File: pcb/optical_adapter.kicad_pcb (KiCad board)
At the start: 2 copper layers, 50 x 20 mm, 15 parts, among them J1 Conn_01x06_Pin, Q1 BC847, Q2 BC847, Q3 BC857, Q4 BC817, U1 LM1117MP-3.3

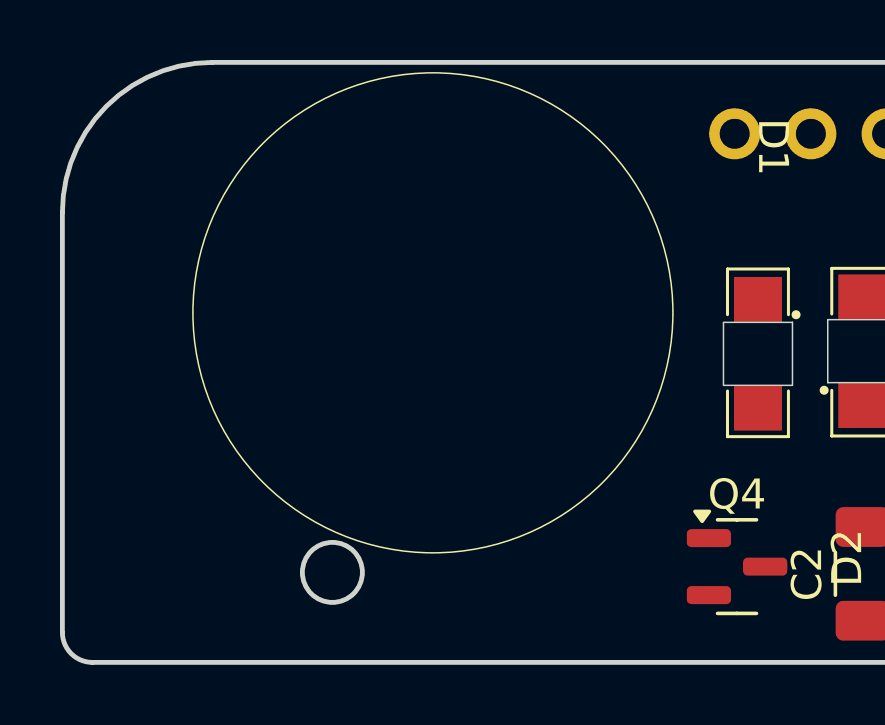
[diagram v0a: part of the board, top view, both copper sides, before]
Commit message: Add PCB coil footprint
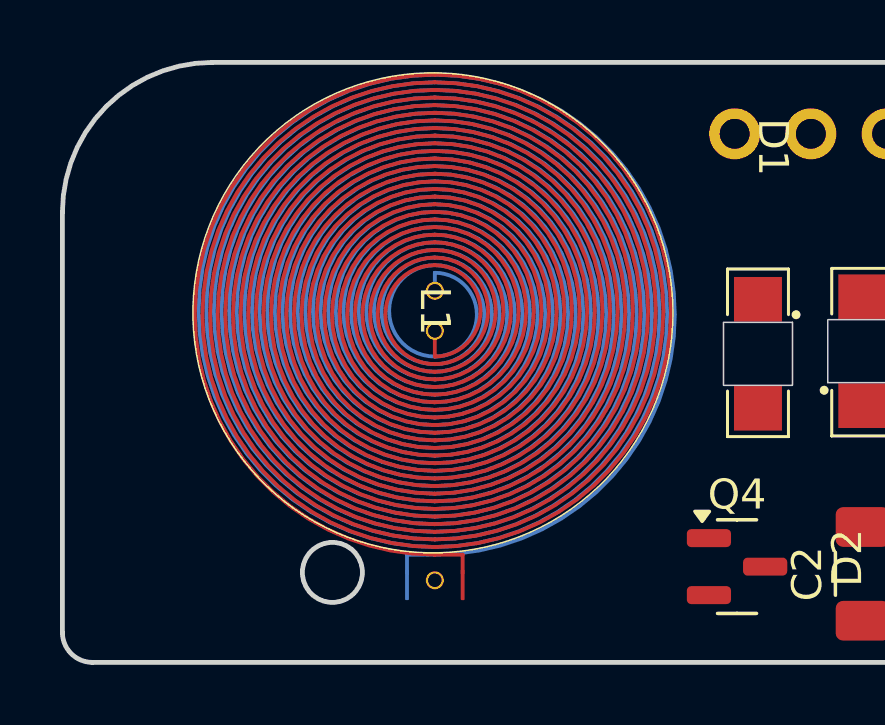
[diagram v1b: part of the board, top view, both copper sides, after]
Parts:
- added L1: L, footprints:26_turn_16_dia_5_mil, F.Cu at (117.0, 95.9)

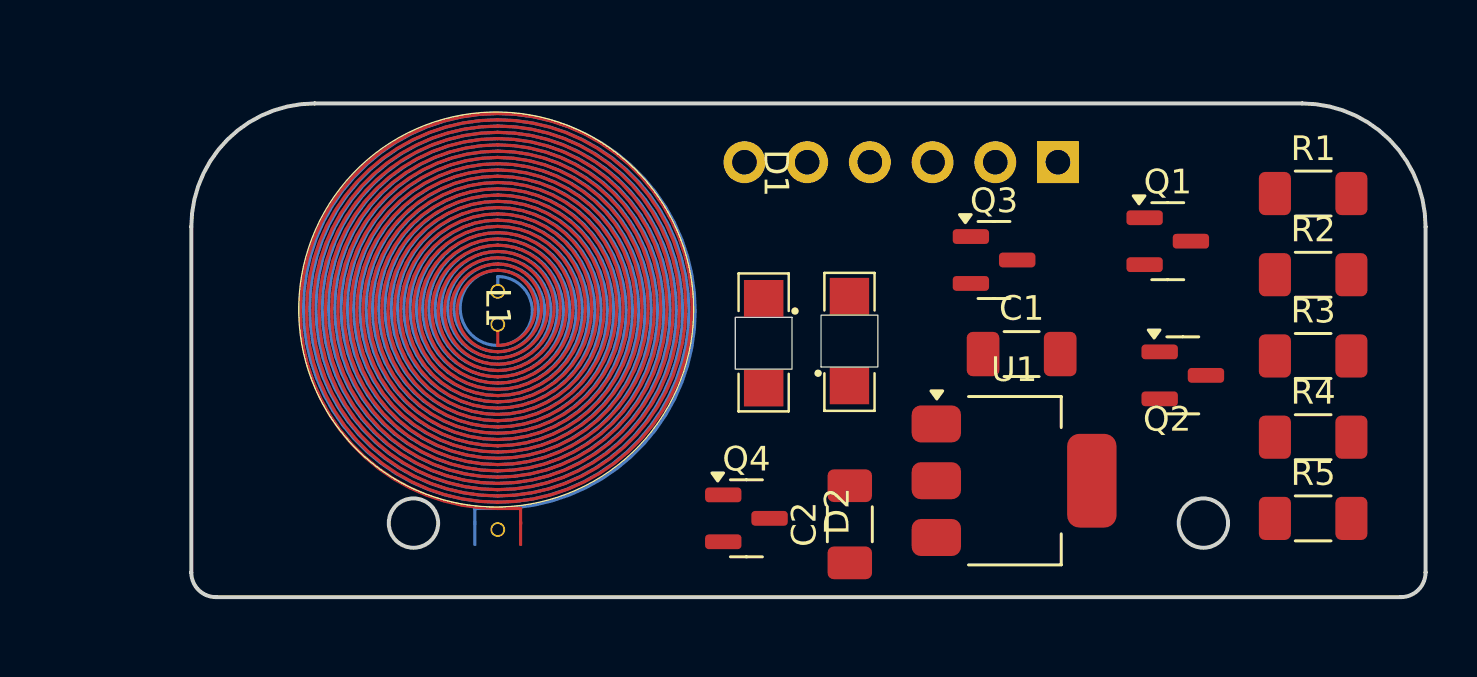
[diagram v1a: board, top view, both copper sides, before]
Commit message: Rough PCB component layout
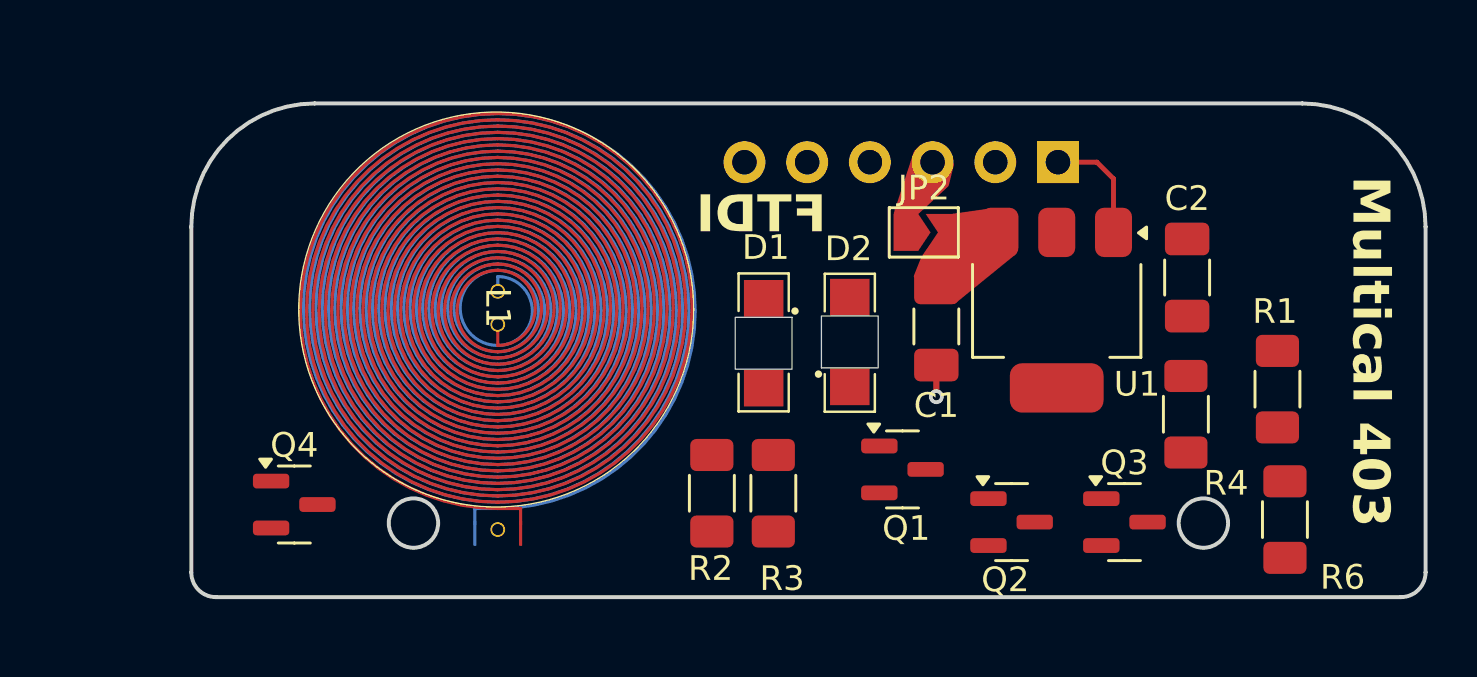
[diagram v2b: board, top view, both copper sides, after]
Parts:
- removed R5: R, Resistor_SMD:R_1206_3216Metric_Pad1.30x1.75mm_HandSolder
- added JP2: SolderJumper_2_Bridged, Jumper:SolderJumper-2_P1.3mm_Open_TrianglePad1.0x1.5mm, F.Cu at (134.2, 92.8)
- added R6: 10k, Resistor_SMD:R_1206_3216Metric_Pad1.30x1.75mm_HandSolder, F.Cu at (148.8, 104.4)
- R1: value R -> 100
- R2: value R -> 15k
- R3: value R -> 39k
- R4: value R -> 10k
- moved R2 25.9 mm to (125.6, 103.4), turned to -90 degrees
- moved R3 22.6 mm to (128.1, 103.4), turned to -90 degrees
- moved Q4 18.3 mm to (108.7, 103.8)
- moved C2 16.9 mm to (144.9, 94.6)
- moved Q1 14.2 mm to (133.3, 102.4)
- moved Q3 11.9 mm to (142.3, 104.5)
- moved Q2 9.13 mm to (137.8, 104.5)
- moved R1 8.06 mm to (148.5, 99.2), turned to 90 degrees
- moved U1 7.12 mm to (139.6, 96.0), turned to -90 degrees
- moved R4 5.24 mm to (144.8, 100.2), turned to -90 degrees
- moved C1 3.63 mm to (134.7, 96.6), turned to -90 degrees
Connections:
- C1 pad 1: unconnected-(C1-Pad1) -> +5V
- C1 pad 2: unconnected-(C1-Pad2) -> GND
- C2 pad 1: unconnected-(C2-Pad1) -> +3V3
- C2 pad 2: unconnected-(C2-Pad2) -> GND
- D1 pad 1: unconnected-(D1-K-Pad1) -> +3V3
- D1 pad 2: unconnected-(D1-A-Pad2) -> /TX
- D2 pad 1: unconnected-(D2-K-Pad1) -> GND
- D2 pad 2: unconnected-(D2-A-Pad2) -> Net-(D2-A)
- J1 pad 3: unconnected-(J1-Pin_3-Pad3) -> VBUS
- Q1 pad 1: unconnected-(Q1-B-Pad1) -> /TX
- Q1 pad 2: unconnected-(Q1-E-Pad2) -> Net-(Q1-E)
- Q1 pad 3: unconnected-(Q1-C-Pad3) -> Net-(Q1-C)
- Q2 pad 1: unconnected-(Q2-B-Pad1) -> Net-(Q1-E)
- Q2 pad 2: unconnected-(Q2-E-Pad2) -> GND
- Q2 pad 3: unconnected-(Q2-C-Pad3) -> /RX
- Q3 pad 1: unconnected-(Q3-B-Pad1) -> Net-(Q3-B)
- Q3 pad 2: unconnected-(Q3-E-Pad2) -> +3V3
- Q3 pad 3: unconnected-(Q3-C-Pad3) -> Net-(Q3-C)
- R1 pad 1: unconnected-(R1-Pad1) -> Net-(Q3-C)
- R1 pad 2: unconnected-(R1-Pad2) -> Net-(D2-A)
- R2 pad 1: unconnected-(R2-Pad1) -> /TX
- R2 pad 2: unconnected-(R2-Pad2) -> GND
- R3 pad 1: unconnected-(R3-Pad1) -> /TX
- R3 pad 2: unconnected-(R3-Pad2) -> Net-(Q3-B)
- R4 pad 1: unconnected-(R4-Pad1) -> +3V3
- R4 pad 2: unconnected-(R4-Pad2) -> Net-(Q1-C)
- U1 pad 1: unconnected-(U1-GND-Pad1) -> GND
- U1 pad 2: unconnected-(U1-VO-Pad2) -> +3V3
- U1 pad 3: unconnected-(U1-VI-Pad3) -> +5V
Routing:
- net GND: track 0.00 -> 5.98 mm, vias 0 -> 1
- added copper zone on In2.Cu, net +3V3
- added copper zone on In1.Cu, net GND
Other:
- copper layers 2 -> 4
- board text added: "FTDI"
- board text added: "Multical 403"

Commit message: Update layout with coil driver components
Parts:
- removed Q4: BC817, Package_TO_SOT_SMD:SOT-23
- added D3: LED, LED_SMD:LED_1206_3216Metric_Pad1.42x1.75mm_HandSolder, F.Cu at (108.8, 104.3)
- added D4: LED, LED_SMD:LED_1206_3216Metric_Pad1.42x1.75mm_HandSolder, F.Cu at (145.6, 89.6)
- added Q5: IRLML2060, Package_TO_SOT_SMD:SOT-23, F.Cu at (106.9, 99.4)
- added R5: 10k, Resistor_SMD:R_1206_3216Metric_Pad1.30x1.75mm_HandSolder, F.Cu at (106.3, 94.7)
- added R7: 220, Resistor_SMD:R_1206_3216Metric_Pad1.30x1.75mm_HandSolder, F.Cu at (107.8, 90.9)
- added R8: 91, Resistor_SMD:R_1206_3216Metric_Pad1.30x1.75mm_HandSolder, F.Cu at (106.3, 104.2)
- added R9: 5.6, Resistor_SMD:R_1206_3216Metric_Pad1.30x1.75mm_HandSolder, F.Cu at (149.4, 90.9)
- moved L1 0.81 mm to (117.8, 96.0), turned to 180 degrees
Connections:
- J1 pad 2: unconnected-(J1-Pin_2-Pad2) -> /WAKE
- J1 pad 4: unconnected-(J1-Pin_4-Pad4) -> /TX
- J1 pad 5: unconnected-(J1-Pin_5-Pad5) -> /RX
- L1 pad 1: unconnected-(L1-Pad1) -> +5V
- L1 pad 2: unconnected-(L1-Pad2) -> Net-(Q5-D)
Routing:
- net VBUS: track 0.00 -> 44.9 mm, vias 0 -> 1
- net Net-(D3-A): track 0.00 -> 2.49 mm
- net GND: track 5.98 -> 8.35 mm, vias 1 -> 2
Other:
- board text removed: "FTDI"

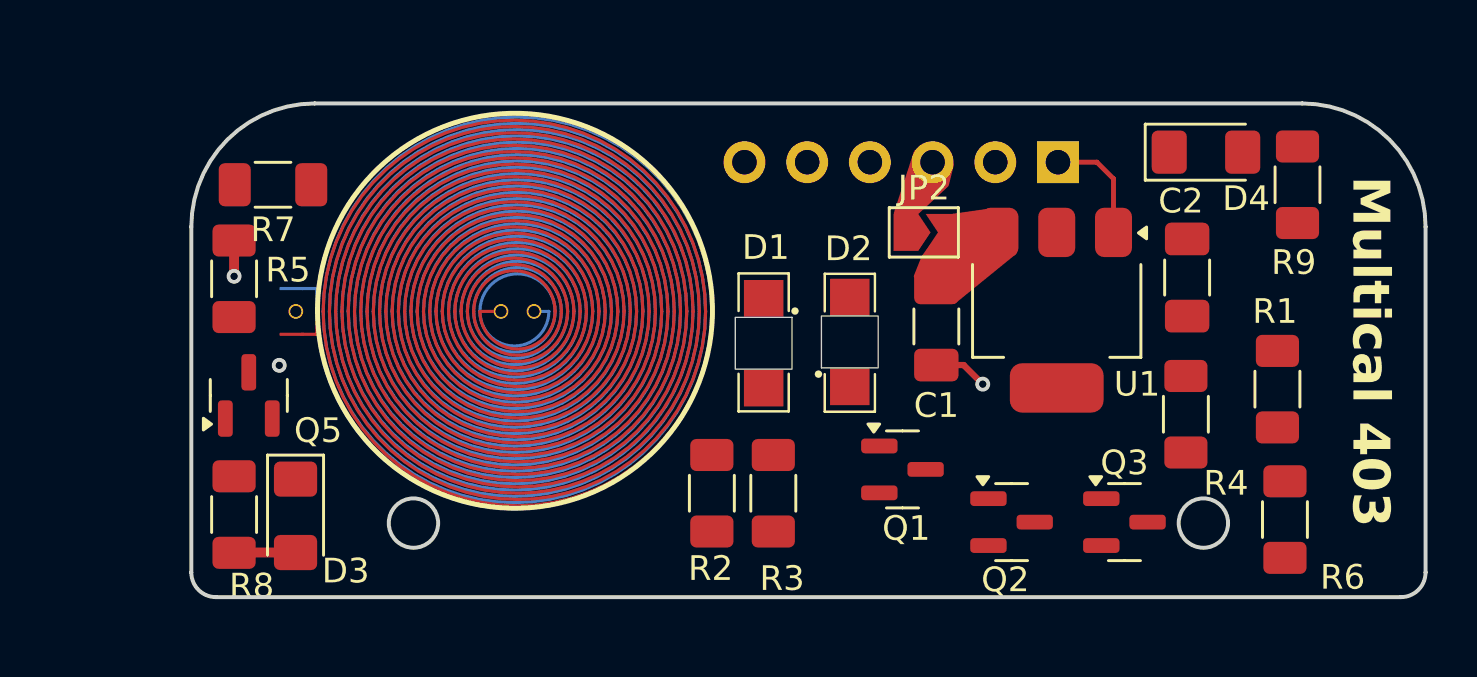
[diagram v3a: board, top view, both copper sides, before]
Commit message: Route power supply
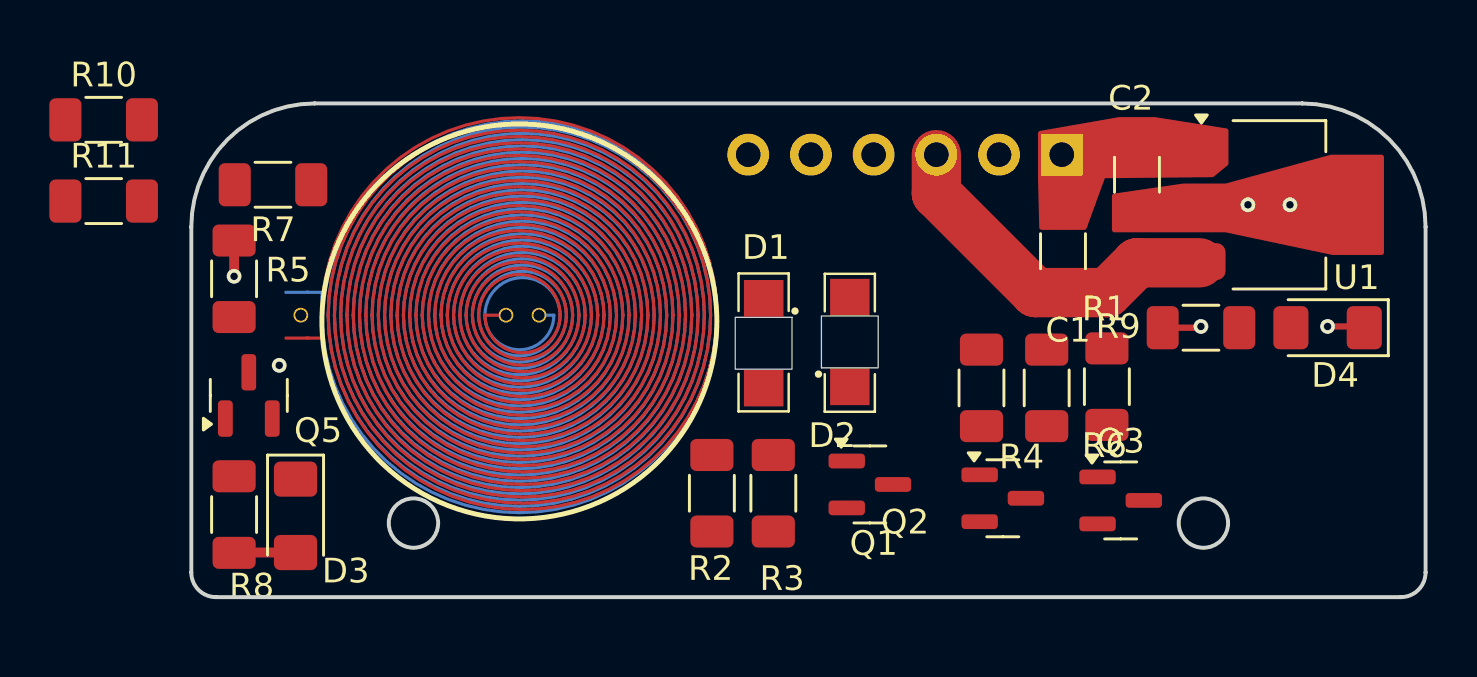
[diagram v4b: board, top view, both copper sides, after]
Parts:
- removed JP2: SolderJumper_2_Bridged, Jumper:SolderJumper-2_P1.3mm_Open_TrianglePad1.0x1.5mm
- added R10: 0, Resistor_SMD:R_1206_3216Metric_Pad1.30x1.75mm_HandSolder, F.Cu at (101.0, 88.3)
- added R11: 0, Resistor_SMD:R_1206_3216Metric_Pad1.30x1.75mm_HandSolder, F.Cu at (101.0, 91.5)
- moved R6 11.0 mm to (139.2, 99.1)
- moved U1 9.95 mm to (148.6, 91.7), turned to 0 degrees
- moved D4 8.65 mm to (150.6, 96.7), turned to 180 degrees
- moved R4 8.35 mm to (136.6, 99.1)
- moved R9 6.99 mm to (145.4, 96.7), turned to 180 degrees
- moved R1 6.91 mm to (141.6, 99.1)
- moved C1 5.97 mm to (139.9, 93.6), turned to 90 degrees
- moved C2 4.63 mm to (142.8, 90.5)
- moved Q1 1.45 mm to (132.0, 103.0)
- moved Q2 1.03 mm to (137.4, 103.6)
- moved Q3 0.89 mm to (142.2, 103.7)
- moved J1 0.34 mm to (139.8, 89.7)
- moved L1 0.25 mm to (118.0, 96.2)
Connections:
- J1 pad 3: VBUS -> +5V
- L1 pad 1: +5V -> Net-(L1-Pad1)
- L1 pad 2: Net-(Q5-D) -> Net-(L1-Pad2)
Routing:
- net +5V: track 0.00 -> 59.4 mm, vias 0 -> 1
- net VBUS: track 44.9 -> 0.00 mm, vias 1 -> 0
- net GND: track 8.35 -> 3.15 mm
- net +3V3: track 0.00 -> 1.51 mm, vias 0 -> 3
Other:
- board text removed: "Multical 403"

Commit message: Update PCB layout
All traces are routed.
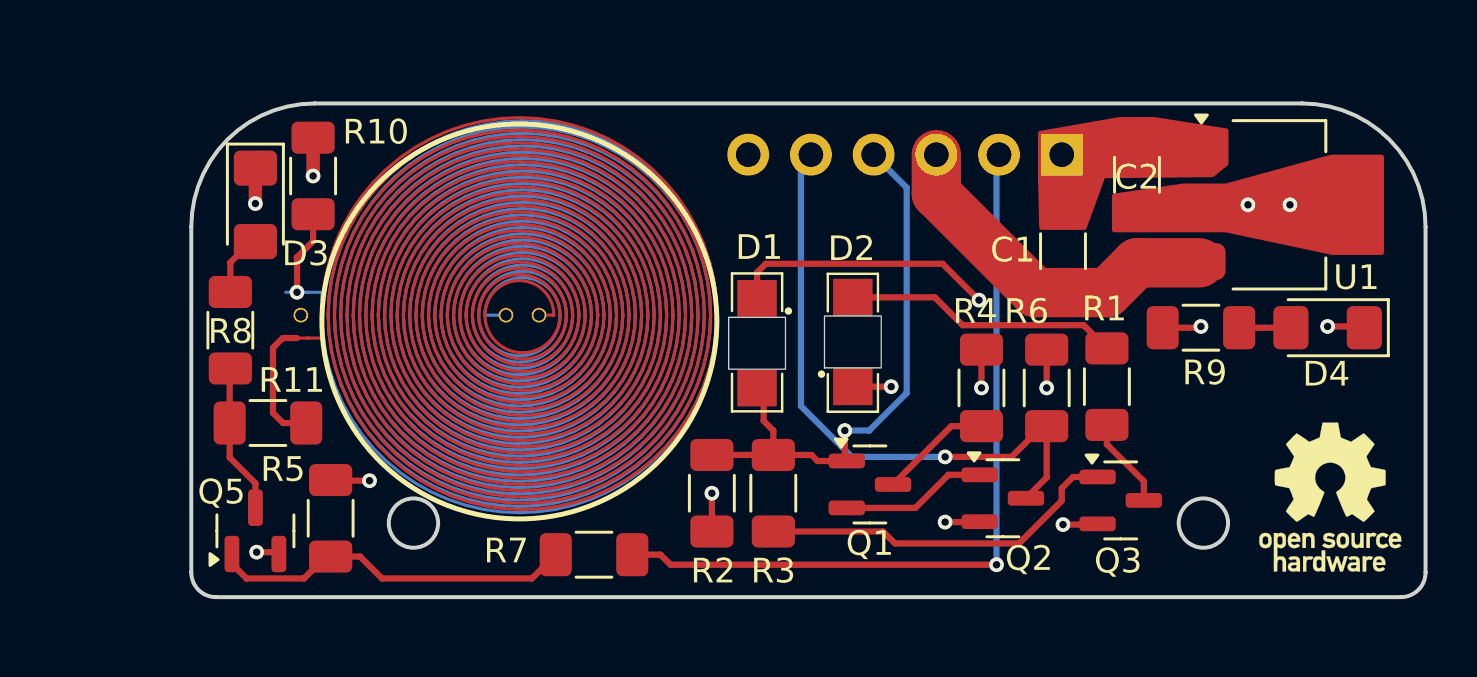
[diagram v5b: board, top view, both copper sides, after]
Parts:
- added REF**: OSHW-Logo_5.7x6mm_SilkScreen, Symbol:OSHW-Logo_5.7x6mm_SilkScreen, F.Cu at (150.7, 103.5)
- L1: moved to B.Cu
- moved R7 19.8 mm to (120.9, 105.9)
- moved D3 12.7 mm to (107.1, 91.7)
- moved R11 11.2 mm to (107.6, 100.5), turned to 180 degrees
- moved R5 10.5 mm to (110.2, 104.4)
- moved R10 8.78 mm to (109.5, 90.5), turned to -90 degrees
- moved R8 7.47 mm to (106.1, 96.8), turned to -90 degrees
- moved Q5 5.49 mm to (107.1, 104.9)
- moved D1 0.27 mm to (130.0, 92.9)
- moved D2 0.12 mm to (128.8, 101.6)
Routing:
- net +5V: track 59.4 -> 17.5 mm, vias 1 -> 2
- net /WAKE: track 0.00 -> 31.6 mm, vias 0 -> 1
- net /RX: track 0.00 -> 24.9 mm, vias 0 -> 1
- net /TX: track 0.00 -> 23.1 mm, vias 0 -> 1
- net +3V3: track 1.51 -> 16.8 mm, vias 3 -> 7
- net Net-(Q5-G): track 0.00 -> 14.9 mm
- net Net-(Q3-B): track 0.00 -> 14.7 mm
- net Net-(D2-A): track 0.00 -> 11.2 mm
- net Net-(Q5-D): track 0.00 -> 6.08 mm
- net Net-(Q1-E): track 0.00 -> 5.94 mm
- net GND: track 3.15 -> 8.84 mm, vias 2 -> 6
- net Net-(L1-Pad2): track 0.00 -> 5.29 mm
- net Net-(Q1-C): track 0.00 -> 4.56 mm
- net Net-(Q3-C): track 0.00 -> 3.68 mm
- net Net-(L1-Pad1): track 0.00 -> 3.44 mm, vias 0 -> 1
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- added copper zone on In2.Cu, net +5V
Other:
- board text added: "NC RX TX 5V WAKE GND"
- board text added: "R0 2025"
- board text added: "https://github.com/Andreasdahlberg/multical-403-optical-adapter"
